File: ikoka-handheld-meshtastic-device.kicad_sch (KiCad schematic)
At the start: 40 parts, among them J1 Conn_Coaxial, J4 1.25-2PWB, Q1 AO3401A, SW1 SW_Push, SW2 SW_Push, U1 MT3608, U2 E22-900M30S, U3 XIAO-nRF52840-SMD, U4 TP4056-42-ESOP8

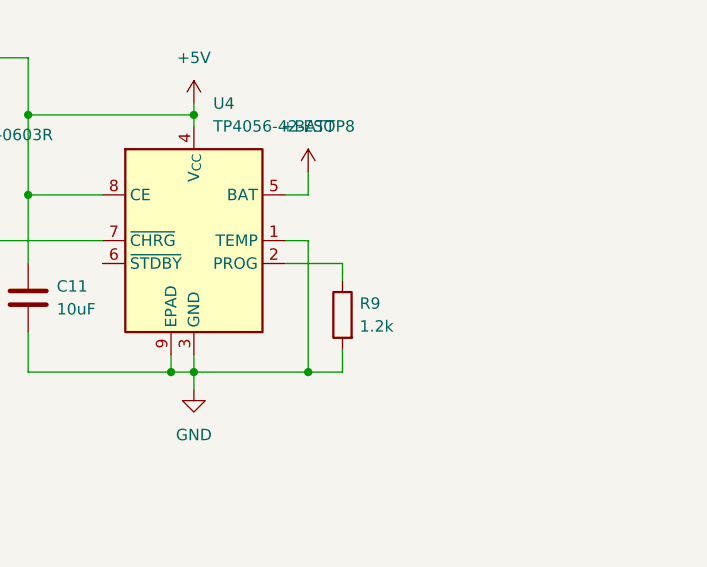
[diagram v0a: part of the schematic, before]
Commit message: fix: Add BAT output capacitor on TP4056
Signed-off-by: Andrew Yong <me@ndoo.sg>
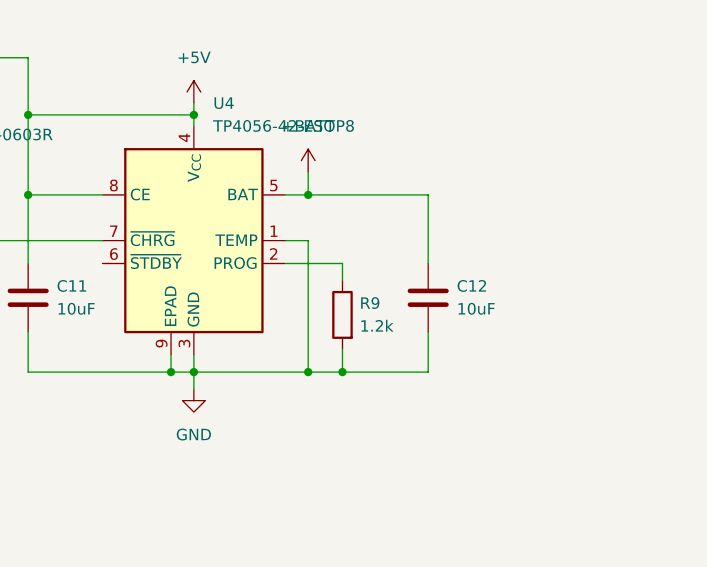
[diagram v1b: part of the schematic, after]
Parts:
- added C12: 10uF, Capacitor_SMD:C_0603_1608Metric, symbol Device:C
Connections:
- net +BATT: now also C12.1
- net GND: now also C12.2
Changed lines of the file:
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@@
 	)
 	(junction
+		(at 245.11 135.255)
+		(diameter 0)
+		(color 0 0 0 0)
+	)
+	(junction
 		(at 143.51 153.67)
 		(diameter 0)
@@
 	)
 	(junction
+		(at 241.3 115.57)
+		(diameter 0)
+		(color 0 0 0 0)
+	)
+	(junction
 		(at 241.3 135.255)
 		(diameter 0)
@@
 	(wire
 		(pts
+			(xy 254.635 135.255) (xy 245.11 135.255)
+		)
+		(stroke
+			(width 0)
+			(type default)
+		)
+	)
+	(wire
+		(pts
 			(xy 210.185 130.81) (xy 210.185 135.255)
 		)
@@
 	(wire
 		(pts
+			(xy 254.635 115.57) (xy 241.3 115.57)
+		)
+		(stroke
+			(width 0)
+			(type default)
+		)
+	)
+	(wire
+		(pts
 			(xy 156.21 101.6) (xy 156.21 99.06)
 		)
@@
 	(wire
 		(pts
+			(xy 254.635 123.19) (xy 254.635 115.57)
+		)
+		(stroke
+			(width 0)
+			(type default)
+		)
+	)
+	(wire
+		(pts
 			(xy 143.51 130.81) (xy 146.05 130.81)
 		)
@@
 	(wire
 		(pts
+			(xy 254.635 130.81) (xy 254.635 135.255)
+		)
+		(stroke
+			(width 0)
+			(type default)
+		)
+	)
+	(wire
+		(pts
 			(xy 143.51 143.51) (xy 143.51 140.97)
 		)
@@
 					(unit 1)
 				)
+			)
+		)
+	)
+	(symbol
+		(lib_id "Device:C")
+		(at 254.635 127 0)
+		(unit 1)
+		(exclude_from_sim no)
+		(in_bom yes)
+		(on_board yes)
+		(dnp no)
+		(fields_autoplaced yes)
+		(property "Reference" "C12"
+			(at 257.81 125.7299 0)
+			(effects
+				(font
+					(size 1.27 1.27)
+				)
+				(justify left)
+			)
+		)
+		(property "Value" "10uF"
+			(at 257.81 128.2699 0)
+			(effects
+				(font
+					(size 1.27 1.27)
+				)
+				(justify left)
+			)
+		)
+		(property "Footprint" "Capacitor_SMD:C_0603_1608Metric"
+			(at 255.6002 130.81 0)
+			(effects
+				(font
+					(size 1.27 1.27)
+				)
+				(hide yes)
+			)
+		)
+		(property "Datasheet" "~"
+			(at 254.635 127 0)
+			(effects
+				(font
+					(size 1.27 1.27)
+				)
+				(hide yes)
+			)
+		)
+		(property "Description" "Unpolarized capacitor"
+			(at 254.635 127 0)
+			(effects
+				(font
+					(size 1.27 1.27)
+				)
+				(hide yes)
+			)
+		)
+		(property "LCSC" "C59461"
+			(at 258.445 125.7299 0)
+			(effects
+				(font
+					(size 1.27 1.27)
+				)
+				(hide yes)
+			)
+		)
+		(pin "1"
+		)
+		(pin "2"
+		)
+		(instances
+			(project "ikoka-handheld-meshtastic-device"
+				(path "/d817f34c-2aa5-4c70-878b-29719eb987fe"
+					(reference "C12")
+					(unit 1)
+				)

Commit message: fix: Flip SSD1306 footprint (fixes #1)
Signed-off-by: Andrew Yong <me@ndoo.sg>
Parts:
- DS1: footprint Display:OLED-128O064D -> Display:OLED-128O064D_ReverseMount
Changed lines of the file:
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@@
 			)
 		)
-		(property "Footprint" "Display:OLED-128O064D"
+		(property "Footprint" "Display:OLED-128O064D_ReverseMount"
 			(at 158.75 146.05 0)
 			(effects

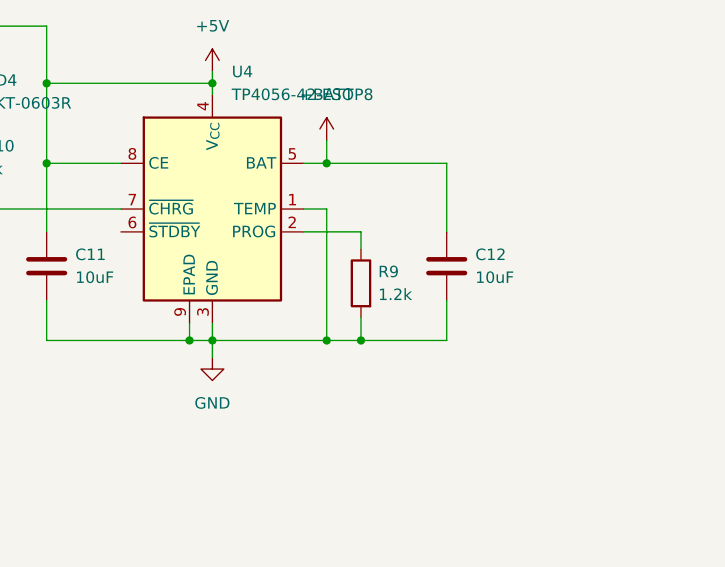
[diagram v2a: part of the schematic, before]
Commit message: feat: Change TP4056 charge current from 1A to 780mA
For a total of 880mA (780mA TP4056 + 100mA onboard XIAO charger).

Most pouch cells the size of the PCB are around 1000mAh, and 1.1A charge rate is above 1C for these cells, which will increase battery wear.

Signed-off-by: Andrew Yong <me@ndoo.sg>
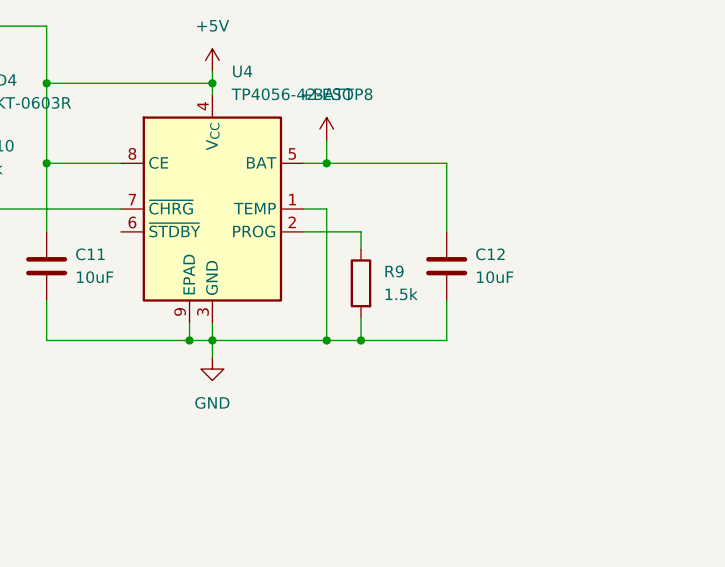
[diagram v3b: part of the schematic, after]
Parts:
- R9: value 1.2k -> 1.5k
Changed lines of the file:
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@@
 		(fields_autoplaced yes)
 		(property "Reference" "R9"
-			(at 247.015 127.6349 0)
+			(at 247.65 127.6349 0)
 			(effects
 				(font
@@
 			)
 		)
-		(property "Value" "1.2k"
-			(at 247.015 130.1749 0)
+		(property "Value" "1.5k"
+			(at 247.65 130.1749 0)
 			(effects
 				(font

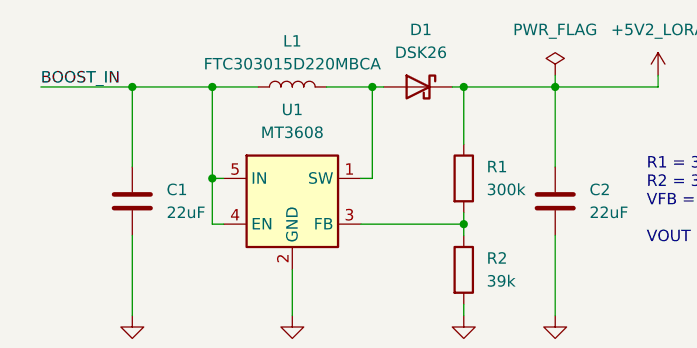
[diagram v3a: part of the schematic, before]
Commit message: fix: Change inductor from 22uH to 2.2uH, Move XIAO up 0.1mm
- Change inductor from 22uH to 2.2uH
  - From: FTC303015D220MBCA
  - To: FNR3015S2R2MT
  - Lower DCR
  - Higher current headroom
  - Better transient response
- Move XIAO module up 0.1mm for better PCB edge clearance

Signed-off-by: Andrew Yong <me@ndoo.sg>
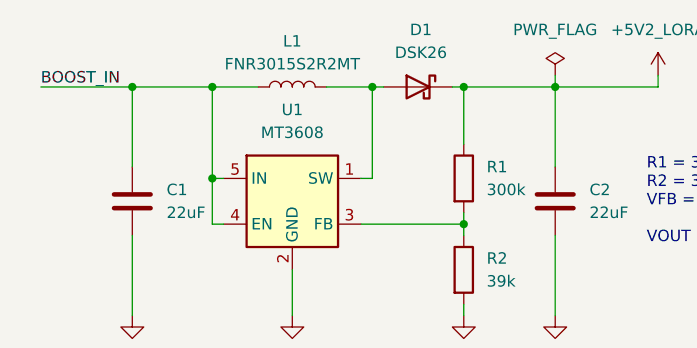
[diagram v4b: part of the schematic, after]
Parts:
- L1: value FTC303015D220MBCA -> FNR3015S2R2MT; footprint Inductor_SMD:L_Wuerth_MAPI-3015 -> Inductor_SMD:L_Changjiang_FNR3015S
- U3: footprint Seeed Studio XIAO Series Library:XIAO-nRF52840-SMD -> Seeed Studio XIAO Series Library:XIAO-nRF52840-SMD_Handsoldering
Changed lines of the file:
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@@
 			)
 		)
-		(property "Value" "FTC303015D220MBCA"
+		(property "Value" "FNR3015S2R2MT"
 			(at 45.72 22.86 90)
 			(effects
@@
 			)
 		)
-		(property "Footprint" "Inductor_SMD:L_Wuerth_MAPI-3015"
+		(property "Footprint" "Inductor_SMD:L_Changjiang_FNR3015S"
 			(at 45.72 25.4 0)
 			(effects
@@
 			)
 		)
-		(property "Footprint" "Seeed Studio XIAO Series Library:XIAO-nRF52840-SMD"
+		(property "Footprint" "Seeed Studio XIAO Series Library:XIAO-nRF52840-SMD_Handsoldering"
 			(at 41.91 160.02 0)
 			(effects

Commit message: chore: Clear ERC and DRC errors/warnings
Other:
- moved on the sheet: C11, C12, C3, C4, D3, D4, J1, J4, Q1, R10, R3, R4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

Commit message: chore: Update JLCPCB parts selection based on preceding changes
Signed-off-by: Andrew Yong <me@ndoo.sg>
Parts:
- C10, C7: value 2.2uF -> 4.7uF
- R5: value 270k -> 300k
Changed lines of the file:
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@@
 			)
 		)
-		(property "Value" "270k"
+		(property "Value" "300k"
 			(at 135.89 182.8799 0)
 			(effects
@@
 			)
 		)
-		(property "Value" "2.2uF"
+		(property "Value" "4.7uF"
 			(at 147.32 182.8799 0)
 			(effects
@@
 			)
 		)
-		(property "Value" "2.2uF"
+		(property "Value" "4.7uF"
 			(at 129.54 144.7799 0)
 			(effects

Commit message: feat(eeschema): Change MT3608 to MT3608B (newer part)
Signed-off-by: Andrew Yong <me@ndoo.sg>
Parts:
- U1: value MT3608 -> MT3608B
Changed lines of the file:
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@@
 			)
 		)
-		(property "Value" "MT3608"
+		(property "Value" "MT3608B"
 			(at 45.72 30.48 0)
 			(effects

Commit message: fix: OLED did not need to be mirrored, add pin 1 & 30 silk
Signed-off-by: Andrew Yong <me@ndoo.sg>
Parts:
- DS1: footprint Display:OLED-128O064D_ReverseMount -> Display:OLED-128O064D
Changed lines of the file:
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@@
 			)
 		)
-		(property "Footprint" "Display:OLED-128O064D_ReverseMount"
+		(property "Footprint" "Display:OLED-128O064D"
 			(at 158.75 146.05 0)
 			(effects
